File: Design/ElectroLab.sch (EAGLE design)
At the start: 229 parts, among them IC11 PAM8403, IC13 74HC08DD, IC14 74HC04DD, IC15 74HC32S14-13, IC3 LM324DTD, IC4 LM324DTD, IC6 MC74HC112ADR2G, IC7 MC74HC112ADR2G, IC8 TLC555CDR, IC9 TP4056, P1 SLIDE_POT_20MM, P2 ALPS_RK09K_VERTICAL, P3 ALPS_RK09K_VERTICAL, T1 MMBT2222A, T2 T_NPNMMBT2222A-1P_CHANGJ_SOT2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, T3 T_NPNMMBT2222A-1P_CHANGJ_SOT2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, T4 T_PNPMMBT5401_CHANGJ_SOT23-BEC, T5 T_PNPMMBT5401_CHANGJ_SOT23-BEC, U1 ADXL335, U2 GAS_SENSOR, U3 AMS1117-3.3VSMD, X8 USB-C-POWER

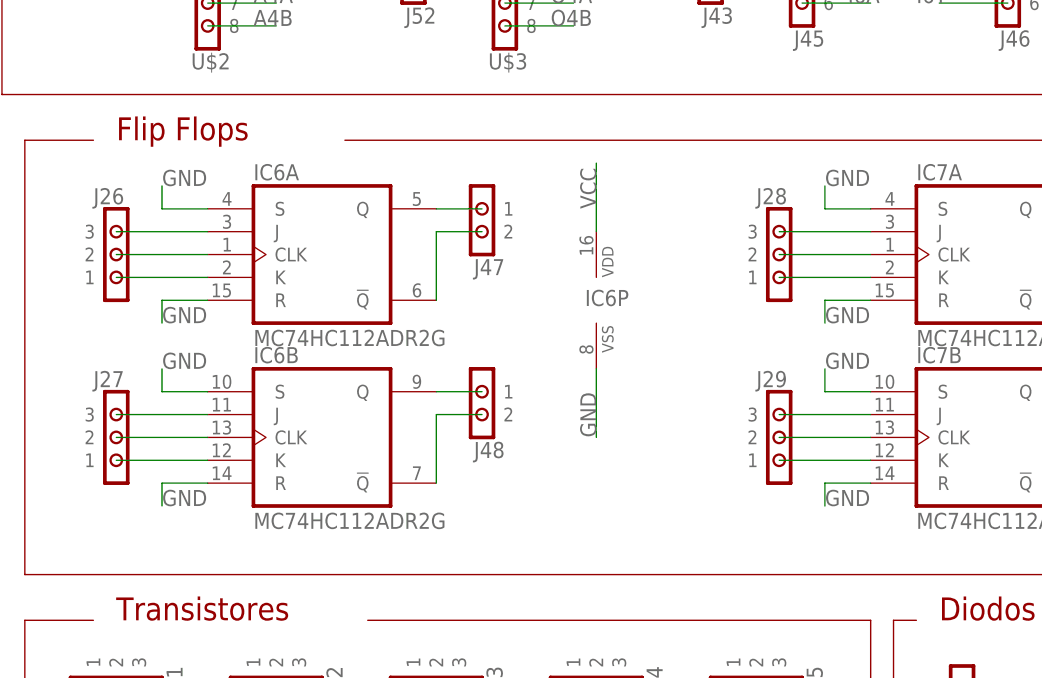
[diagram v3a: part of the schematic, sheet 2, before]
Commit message: Set & reset connected to VCC (3.3V) instead of GND
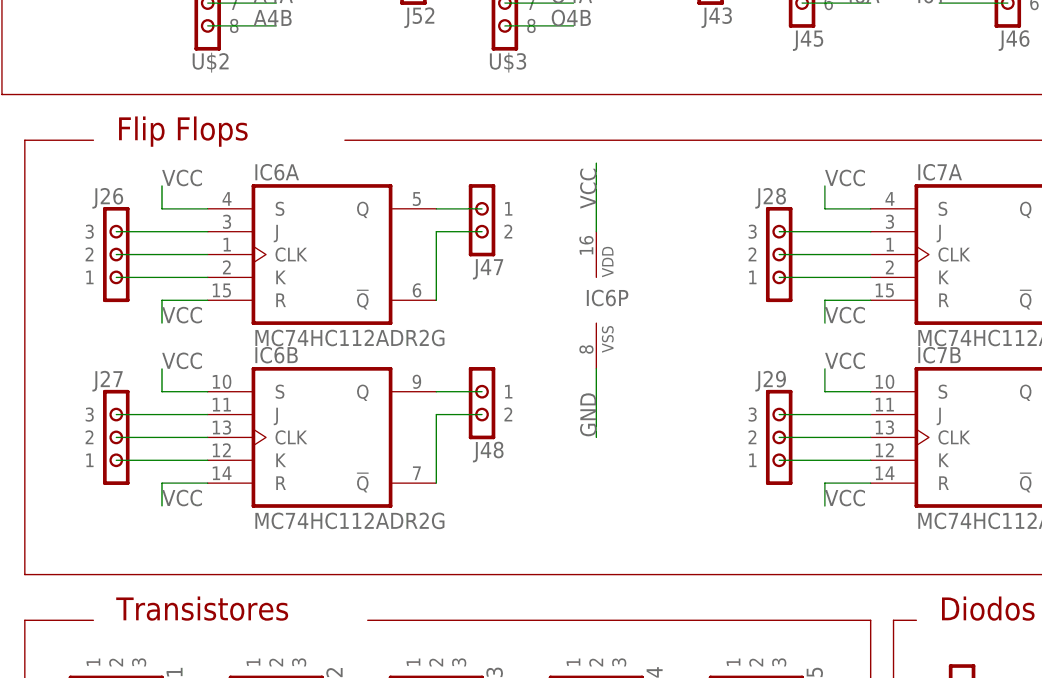
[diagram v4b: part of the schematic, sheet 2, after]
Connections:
- net GND: no longer IC6A.R, IC6A.S, IC6B.R, IC6B.S, IC7A.R, IC7A.S, IC7B.R, IC7B.S
- net VCC: now also IC6A.R, IC6A.S, IC6B.R, IC6B.S, IC7A.R, IC7A.S, IC7B.R, IC7B.S
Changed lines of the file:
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@@
 <label x="147.32" y="76.2" size="1.778" layer="95" rot="R90"/>
+</segment>
+<segment>
+<pinref part="IC6" gate="A" pin="S"/>
+<wire x1="30.48" y1="78.74" x2="25.4" y2="78.74" width="0.1524" layer="91"/>
+<wire x1="25.4" y1="78.74" x2="25.4" y2="81.28" width="0.1524" layer="91"/>
+<label x="25.4" y="81.28" size="1.778" layer="95"/>
+</segment>
+<segment>
+<pinref part="IC6" gate="A" pin="R"/>
+<wire x1="30.48" y1="68.58" x2="25.4" y2="68.58" width="0.1524" layer="91"/>
+<wire x1="25.4" y1="68.58" x2="25.4" y2="66.04" width="0.1524" layer="91"/>
+<label x="25.4" y="66.04" size="1.778" layer="95"/>
+</segment>
+<segment>
+<pinref part="IC6" gate="B" pin="S"/>
+<wire x1="30.48" y1="58.42" x2="25.4" y2="58.42" width="0.1524" layer="91"/>
+<wire x1="25.4" y1="58.42" x2="25.4" y2="60.96" width="0.1524" layer="91"/>
+<label x="25.4" y="60.96" size="1.778" layer="95"/>
+</segment>
+<segment>
+<pinref part="IC6" gate="B" pin="R"/>
+<wire x1="30.48" y1="48.26" x2="25.4" y2="48.26" width="0.1524" layer="91"/>
+<wire x1="25.4" y1="48.26" x2="25.4" y2="45.72" width="0.1524" layer="91"/>
+<label x="25.4" y="45.72" size="1.778" layer="95"/>
+</segment>
+<segment>
+<pinref part="IC7" gate="A" pin="S"/>
+<wire x1="104.14" y1="78.74" x2="99.06" y2="78.74" width="0.1524" layer="91"/>
+<wire x1="99.06" y1="78.74" x2="99.06" y2="81.28" width="0.1524" layer="91"/>
+<label x="99.06" y="81.28" size="1.778" layer="95"/>
+</segment>
+<segment>
+<pinref part="IC7" gate="A" pin="R"/>
+<wire x1="104.14" y1="68.58" x2="99.06" y2="68.58" width="0.1524" layer="91"/>
+<wire x1="99.06" y1="68.58" x2="99.06" y2="66.04" width="0.1524" layer="91"/>
+<label x="99.06" y="66.04" size="1.778" layer="95"/>
+</segment>
+<segment>
+<pinref part="IC7" gate="B" pin="S"/>
+<wire x1="104.14" y1="58.42" x2="99.06" y2="58.42" width="0.1524" layer="91"/>
+<wire x1="99.06" y1="58.42" x2="99.06" y2="60.96" width="0.1524" layer="91"/>
+<label x="99.06" y="60.96" size="1.778" layer="95"/>
+</segment>
+<segment>
+<pinref part="IC7" gate="B" pin="R"/>
+<wire x1="104.14" y1="48.26" x2="99.06" y2="48.26" width="0.1524" layer="91"/>
+<wire x1="99.06" y1="48.26" x2="99.06" y2="45.72" width="0.1524" layer="91"/>
+<label x="99.06" y="45.72" size="1.778" layer="95"/>
 </segment>
 </net>
@@
 </segment>
 <segment>
-<pinref part="IC6" gate="A" pin="S"/>
-<wire x1="30.48" y1="78.74" x2="25.4" y2="78.74" width="0.1524" layer="91"/>
-<wire x1="25.4" y1="78.74" x2="25.4" y2="81.28" width="0.1524" layer="91"/>
-<label x="25.4" y="81.28" size="1.778" layer="95"/>
-</segment>
-<segment>
-<pinref part="IC6" gate="A" pin="R"/>
-<wire x1="30.48" y1="68.58" x2="25.4" y2="68.58" width="0.1524" layer="91"/>
-<wire x1="25.4" y1="68.58" x2="25.4" y2="66.04" width="0.1524" layer="91"/>
-<label x="25.4" y="66.04" size="1.778" layer="95"/>
-</segment>
-<segment>
-<pinref part="IC6" gate="B" pin="S"/>
-<wire x1="30.48" y1="58.42" x2="25.4" y2="58.42" width="0.1524" layer="91"/>
-<wire x1="25.4" y1="58.42" x2="25.4" y2="60.96" width="0.1524" layer="91"/>
-<label x="25.4" y="60.96" size="1.778" layer="95"/>
-</segment>
-<segment>
-<pinref part="IC6" gate="B" pin="R"/>
-<wire x1="30.48" y1="48.26" x2="25.4" y2="48.26" width="0.1524" layer="91"/>
-<wire x1="25.4" y1="48.26" x2="25.4" y2="45.72" width="0.1524" layer="91"/>
-<label x="25.4" y="45.72" size="1.778" layer="95"/>
-</segment>
-<segment>
-<pinref part="IC7" gate="A" pin="S"/>
-<wire x1="104.14" y1="78.74" x2="99.06" y2="78.74" width="0.1524" layer="91"/>
-<wire x1="99.06" y1="78.74" x2="99.06" y2="81.28" width="0.1524" layer="91"/>
-<label x="99.06" y="81.28" size="1.778" layer="95"/>
-</segment>
-<segment>
-<pinref part="IC7" gate="A" pin="R"/>
-<wire x1="104.14" y1="68.58" x2="99.06" y2="68.58" width="0.1524" layer="91"/>
-<wire x1="99.06" y1="68.58" x2="99.06" y2="66.04" width="0.1524" layer="91"/>
-<label x="99.06" y="66.04" size="1.778" layer="95"/>
-</segment>
-<segment>
-<pinref part="IC7" gate="B" pin="S"/>
-<wire x1="104.14" y1="58.42" x2="99.06" y2="58.42" width="0.1524" layer="91"/>
-<wire x1="99.06" y1="58.42" x2="99.06" y2="60.96" width="0.1524" layer="91"/>
-<label x="99.06" y="60.96" size="1.778" layer="95"/>
-</segment>
-<segment>
-<pinref part="IC7" gate="B" pin="R"/>
-<wire x1="104.14" y1="48.26" x2="99.06" y2="48.26" width="0.1524" layer="91"/>
-<wire x1="99.06" y1="48.26" x2="99.06" y2="45.72" width="0.1524" layer="91"/>
-<label x="99.06" y="45.72" size="1.778" layer="95"/>
-</segment>
-<segment>

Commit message: Added design files
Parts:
- IC15: device SpaceDIY_IC:74AHC32DD -> SpaceDIY_IC:74AHC32D74HC32S14-13
- S1: device bt_electromech:DPDT_JS202011CQN -> SpaceDIY_electromechanical:DPDT_JS202011CQN
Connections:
- net VBAT: now also S1.R2; no longer S1.R1
- net V_USB: now also S1.L2; no longer S1.L1
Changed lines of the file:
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@@
 <part name="C19" library="SpaceDIY_passive_components" deviceset="C7343" device="" value="470uF"/>
 <part name="C20" library="SpaceDIY_passive_components" deviceset="C7343" device="" value="470uF"/>
-<part name="S1" library="bt_electromech" deviceset="DPDT" device="_JS202011CQN" value=""/>
+<part name="S1" library="SpaceDIY_electromechanical" deviceset="DPDT" device="_JS202011CQN" value="DPDT_JS202011CQN"/>
 <part name="R31" library="SpaceDIY_passive_components" deviceset="R0603" device="" value="470"/>
 <part name="H1" library="holes" library_urn="urn:adsk.eagle:library:237" deviceset="MOUNT-PAD-ROUND" device="2.8" package3d_urn="urn:adsk.eagle:package:14281/1" value="MOUNT-PAD-ROUND2.8"/>
@@
 <part name="IC13" library="SpaceDIY_IC" deviceset="74HC08D" device="D" package3d_urn="urn:adsk.eagle:package:1010/2"/>
 <part name="IC14" library="SpaceDIY_IC" deviceset="74HC04D" device="D" package3d_urn="urn:adsk.eagle:package:1010/2"/>
-<part name="IC15" library="SpaceDIY_IC" deviceset="74AHC32D" device="D" package3d_urn="urn:adsk.eagle:package:1010/2" value="74HC32S14-13">
+<part name="IC15" library="SpaceDIY_IC" deviceset="74AHC32D" device="74HC32S14-13" package3d_urn="urn:adsk.eagle:package:1010/2" value="74HC32S14-13">
 <attribute name="LCSC" value="C176921"/>
 </part>
@@
 <instance part="S1" gate="G$1" x="147.32" y="40.64" smashed="yes" rot="R90">
 <attribute name="NAME" x="143.51" y="36.83" size="1.778" layer="95" rot="R90"/>
-<attribute name="VALUE" x="152.4" y="36.83" size="1.778" layer="96" rot="R90"/>
 </instance>
 <instance part="R31" gate="G$1" x="220.98" y="50.8" smashed="yes">
@@
 </segment>
 <segment>
-<wire x1="144.78" y1="50.8" x2="142.24" y2="50.8" width="0.1524" layer="91"/>
-<label x="142.24" y="50.8" size="1.27" layer="95" rot="R180" xref="yes"/>
-<pinref part="S1" gate="G$1" pin="R1"/>
-<wire x1="144.78" y1="45.72" x2="144.78" y2="50.8" width="0.1524" layer="91"/>
+<pinref part="S1" gate="G$1" pin="R2"/>
+<wire x1="149.86" y1="45.72" x2="149.86" y2="48.26" width="0.1524" layer="91"/>
+<wire x1="149.86" y1="48.26" x2="152.4" y2="48.26" width="0.1524" layer="91"/>
+<label x="152.4" y="48.26" size="1.27" layer="95" xref="yes"/>
 </segment>
 </net>
@@
 </segment>
 <segment>
-<pinref part="S1" gate="G$1" pin="L1"/>
-<wire x1="144.78" y1="35.56" x2="144.78" y2="33.02" width="0.1524" layer="91"/>
-<wire x1="144.78" y1="33.02" x2="142.24" y2="33.02" width="0.1524" layer="91"/>
-<label x="142.24" y="33.02" size="1.27" layer="95" rot="R180" xref="yes"/>
+<wire x1="149.86" y1="33.02" x2="152.4" y2="33.02" width="0.1524" layer="91"/>
+<label x="152.4" y="33.02" size="1.27" layer="95" xref="yes"/>
+<pinref part="S1" gate="G$1" pin="L2"/>
+<wire x1="149.86" y1="33.02" x2="149.86" y2="35.56" width="0.1524" layer="91"/>
 </segment>
 </net>
@@
 <pinref part="S1" gate="G$1" pin="LC"/>
 <wire x1="147.32" y1="35.56" x2="147.32" y2="33.02" width="0.1524" layer="91"/>
-<wire x1="147.32" y1="33.02" x2="149.86" y2="33.02" width="0.1524" layer="91"/>
-<label x="149.86" y="33.02" size="1.27" layer="95" xref="yes"/>
-</segment>
-</net>
+<wire x1="147.32" y1="33.02" x2="144.78" y2="33.02" width="0.1524" layer="91"/>
+<label x="144.78" y="33.02" size="1.27" layer="95" rot="R180" xref="yes"/>
+</segment>
+</net>
